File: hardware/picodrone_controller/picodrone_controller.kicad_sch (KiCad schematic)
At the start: 32 parts, among them J1 RPi Pico, J2 RPi Pico, J3 MPU6050, J4 SD Card, J5 Motor, J6 Motor, J7 Motor, J8 Motor, J9 Battery, Q1 NMOS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

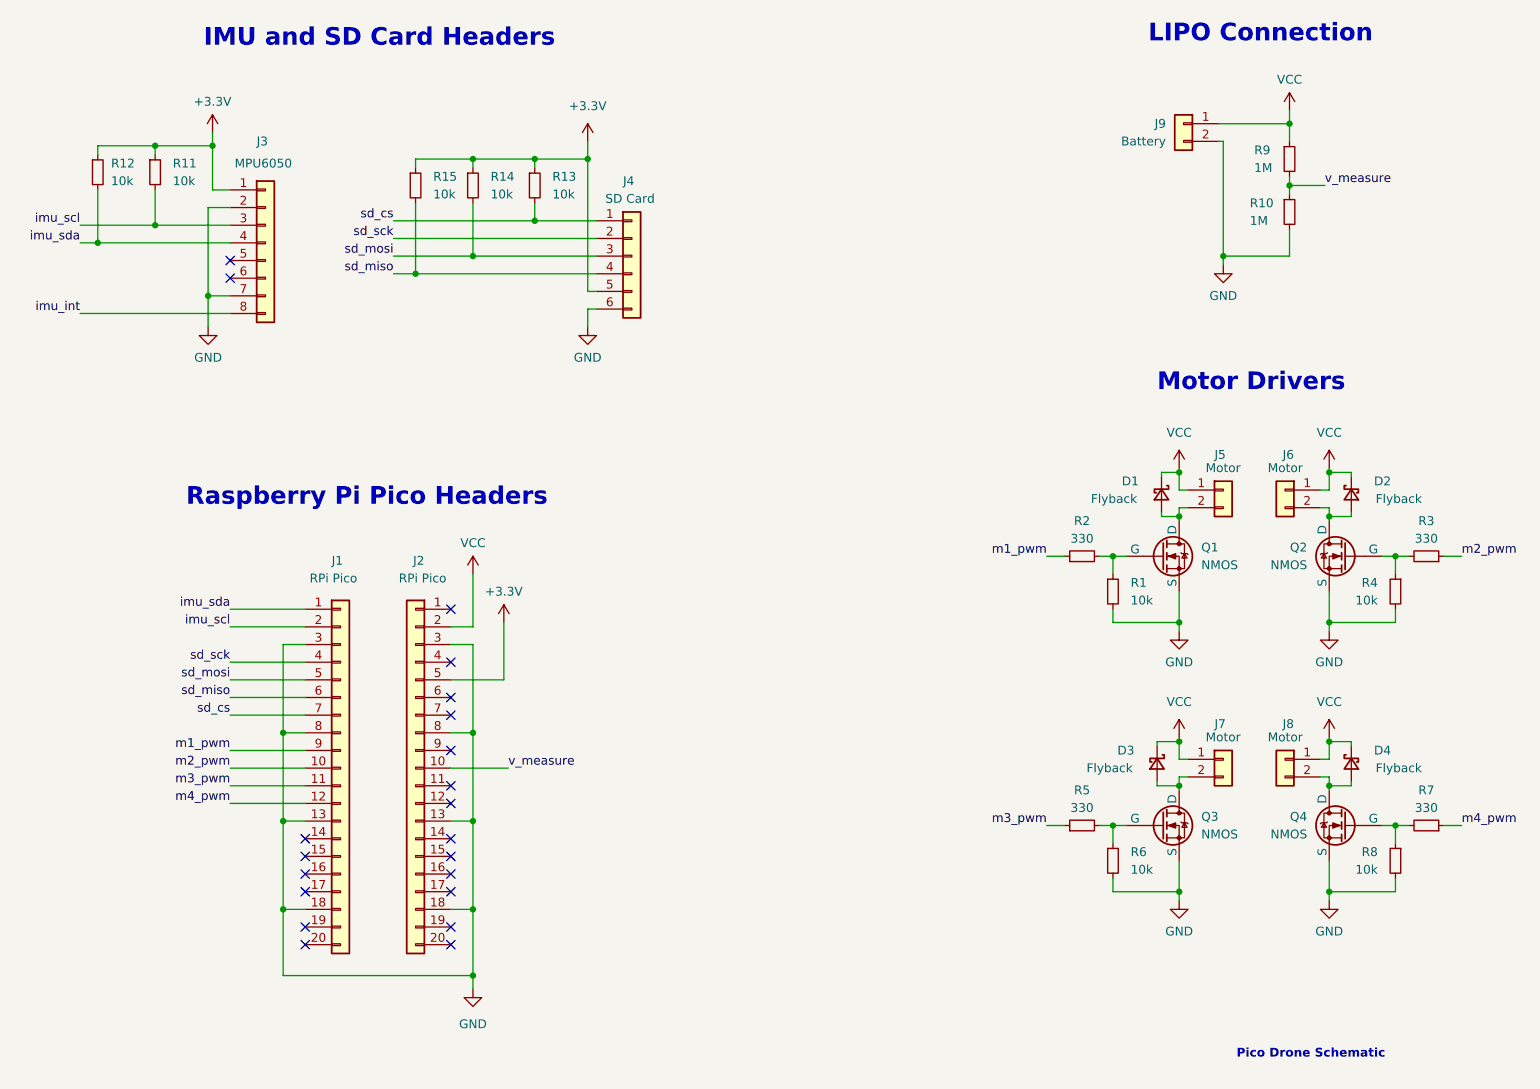
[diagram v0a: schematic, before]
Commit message: rearrange schematic to help with pcb layout
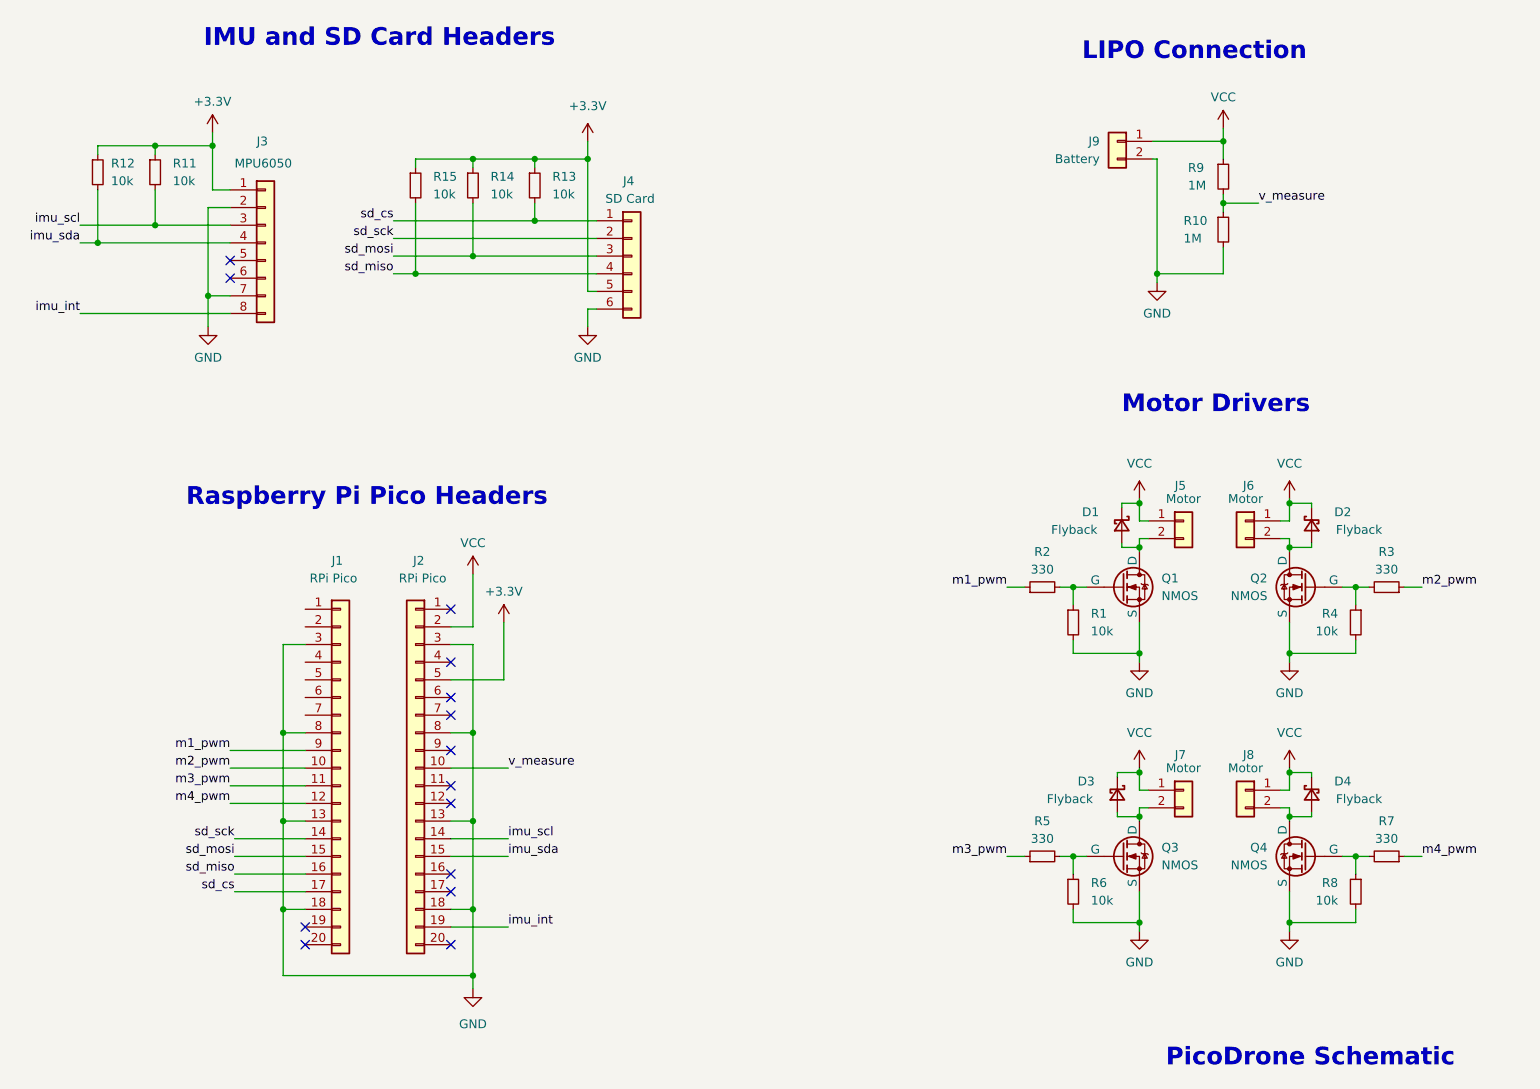
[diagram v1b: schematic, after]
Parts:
- D1, D2, D3, D4: footprint (none) -> schottky_DSS16UTR:SODFL3618X110N
- J1, J2: footprint (none) -> Connector_PinSocket_2.54mm:PinSocket_1x20_P2.54mm_Vertical
- J3: footprint (none) -> Connector_PinSocket_2.54mm:PinSocket_1x08_P2.54mm_Vertical
- J4: footprint (none) -> Connector_PinSocket_2.54mm:PinSocket_1x06_P2.54mm_Vertical
- J5, J6, J7, J8, J9: footprint (none) -> Connector_PinHeader_2.54mm:PinHeader_1x02_P2.54mm_Vertical
- Q1, Q2, Q3, Q4: footprint (none) -> nmos_SI2302CDS-T1-E3:TO-236_VIS
- R1, R10, R11, R12, R13, R14, R15, R2, R3, R4, R5, R6, R7, R8, R9: footprint (none) -> Resistor_SMD:R_0805_2012Metric
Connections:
- net imu_int: now also J2.19 (Pin_19)
- net imu_scl: now also J2.14 (Pin_14); no longer J1.2 (Pin_2)
- net imu_sda: now also J2.15 (Pin_15); no longer J1.1 (Pin_1)
- net sd_cs: now also J1.17 (Pin_17); no longer J1.7 (Pin_7)
- net sd_miso: now also J1.16 (Pin_16); no longer J1.6 (Pin_6)
- net sd_mosi: now also J1.15 (Pin_15); no longer J1.5 (Pin_5)
- net sd_sck: now also J1.14 (Pin_14); no longer J1.4 (Pin_4)
- no-connect marks 21 -> 14
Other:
- note added: "PicoDrone Schematic"
- note removed: "Pico Drone Schematic"
- moved on the sheet: D1, D2, D3, D4, J5, J6, J7, J8, J9, Q1, Q2, Q3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
